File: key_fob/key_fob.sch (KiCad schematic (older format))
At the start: 21 parts

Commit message: Updated schmatic to include alarm off button
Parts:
- removed C? (x2): C, symbol Device:C
- removed U?: AMS1117-3.3, Package_TO_SOT_SMD:SOT-223-3_TabPin2, symbol Regulator_Linear:AMS1117-3.3
- added SW?: SW_DIP_x01, symbol Switch:SW_DIP_x01
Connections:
- net labels added: ALARM_OFF
- wire segments 40 -> 41
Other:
- moved on the sheet: D?, R?, SW?

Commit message: Added footprint and symbol library for some of the parts picked out
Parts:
- removed J?: Conn_01x02_Male, symbol Connector:Conn_01x02_Male
- removed LS?: Speaker, symbol Device:Speaker
- added C?: 2.2u, symbol Device:C
- added C?: 0.1u, symbol Device:C
- added IC?: L4931ABDT33-TR, TO228P972X240-3N, symbol SamacSys:L4931ABDT33-TR
- added J?: B2B-PH-K-S_LF__SN_, digikey-footprints:PinHeader_1x2_P2mm_Drill1mm, symbol digikey-kicad-library:B2B-PH-K-S_LF__SN_
- added U?: PS1240P02BT, PS1240P02BT, symbol PS1240P02BT:PS1240P02BT
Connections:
- net labels added: BUTTON0, POWER_LED
- net labels removed: ALARM_OFF
- wire segments 41 -> 55
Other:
- moved on the sheet: SW?

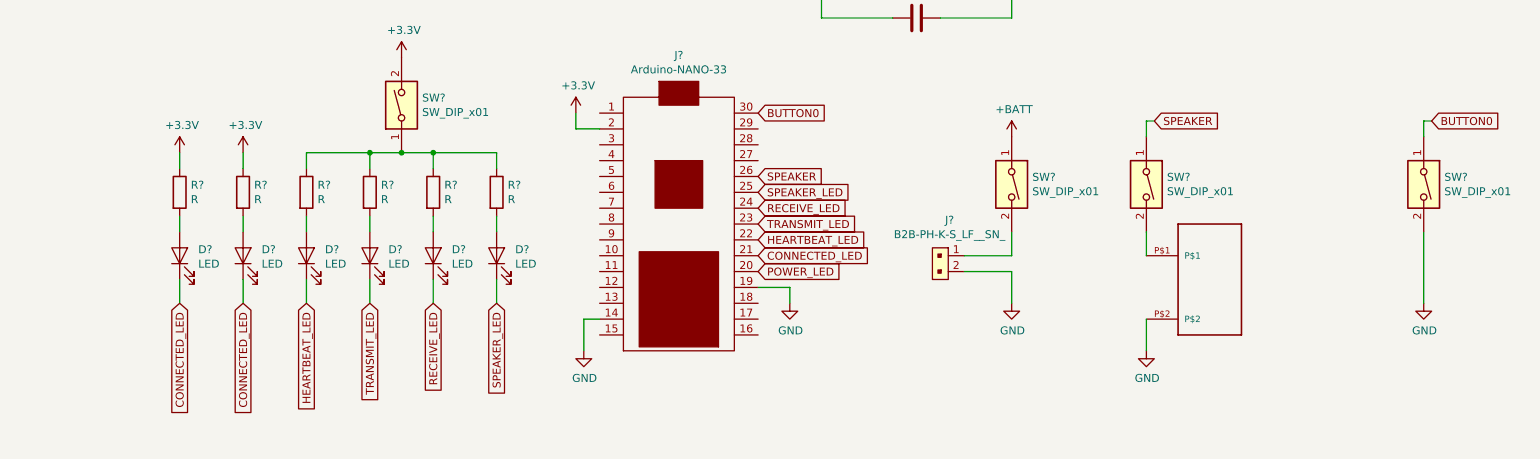
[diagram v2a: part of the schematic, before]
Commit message: Added Mosfets for External LEDs
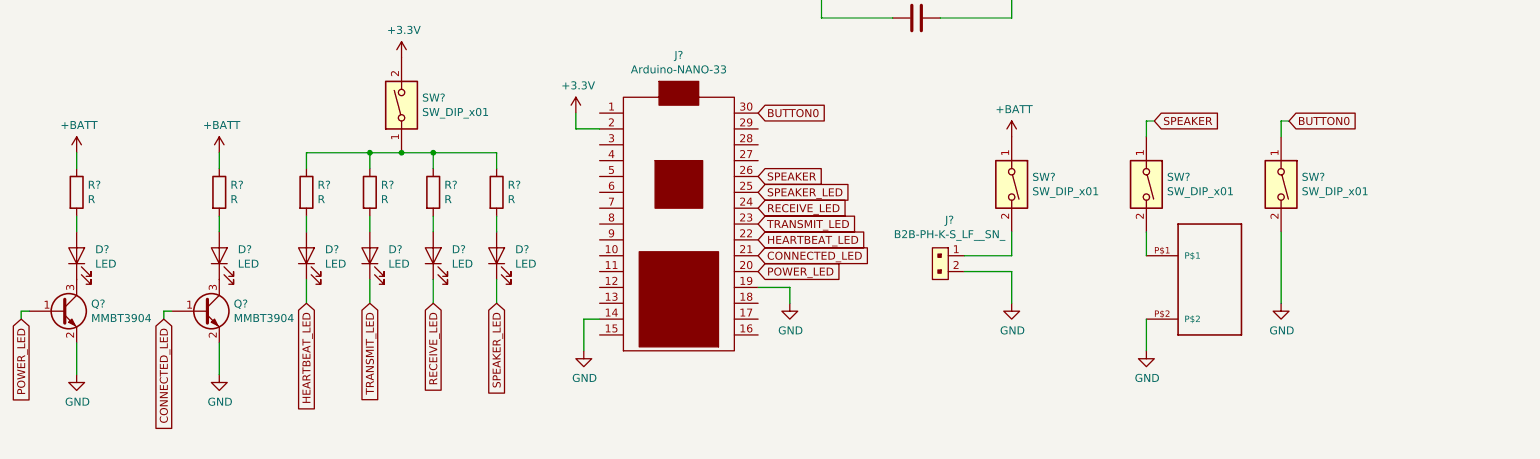
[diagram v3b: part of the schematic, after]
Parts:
- removed D? (x2): LED, symbol Device:LED
- removed R? (x2): R, symbol Device:R
- added D? (x2): LED, symbol Device:LED
- added Q? (x2): MMBT3904, Package_TO_SOT_SMD:SOT-23, symbol Transistor_BJT:MMBT3904
- added R? (x2): R, symbol Device:R
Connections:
- net +BATT: now also R?.1, R?.1
- net CONNECTED_LED: now also Q?.1 (B)
- net GND: now also Q?.2 (E), Q?.2 (E)
- net POWER_LED: now also Q?.1 (B)
- new net: D?.1 (K), Q?.3 (C) (x2)
- new net: D?.2 (A), R?.2 (x2)
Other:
- moved on the sheet: SW?
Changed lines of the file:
@@
 $EndDescr
-$Comp
-L Device:LED D?
-U 1 1 5E30F328
-P 2700 3800
-F 0 "D?" V 2739 3683 50  0000 R CNN
-F 1 "LED" V 2648 3683 50  0000 R CNN
-F 2 "" H 2700 3800 50  0001 C CNN
-F 3 "~" H 2700 3800 50  0001 C CNN
-	1    2700 3800
-	0    -1   -1   0
-$EndComp
-$Comp
-L Device:R R?
-U 1 1 5E3103C7
-P 2700 3400
-F 0 "R?" H 2770 3446 50  0000 L CNN
-F 1 "R" H 2770 3355 50  0000 L CNN
-F 2 "" V 2630 3400 50  0001 C CNN
-F 3 "~" H 2700 3400 50  0001 C CNN
-	1    2700 3400
-	1    0    0    -1
-$EndComp
-Wire Wire Line
-	2700 3550 2700 3650
-Wire Wire Line
-	2700 3250 2700 3150
-$Comp
-L Device:R R?
-U 1 1 5E319CBA
-P 3100 3400
-F 0 "R?" H 3170 3446 50  0000 L CNN
-F 1 "R" H 3170 3355 50  0000 L CNN
-F 2 "" V 3030 3400 50  0001 C CNN
-F 3 "~" H 3100 3400 50  0001 C CNN
-	1    3100 3400
-	1    0    0    -1
-$EndComp
 $Comp
 L Device:R R?
@@
 Wire Wire Line
 	3500 4100 3500 3950
-Wire Wire Line
-	3100 4100 3100 3950
-Text GLabel 3100 4100 3    50   Input ~ 0
+Text GLabel 2600 4200 3    50   Input ~ 0
 CONNECTED_LED
-$Comp
-L Device:LED D?
-U 1 1 5E319CB4
-P 3100 3800
-F 0 "D?" V 3139 3683 50  0000 R CNN
-F 1 "LED" V 3048 3683 50  0000 R CNN
-F 2 "" H 3100 3800 50  0001 C CNN
-F 3 "~" H 3100 3800 50  0001 C CNN
-	1    3100 3800
-	0    -1   -1   0
-$EndComp
-Wire Wire Line
-	3100 3550 3100 3650
 Text GLabel 6350 3600 2    50   Input ~ 0
 TRANSMIT_LED
@@
 Wire Wire Line
 	4700 3250 4700 3150
-$Comp
-L power:+3.3V #PWR?
-U 1 1 5E33A695
-P 2700 3150
-F 0 "#PWR?" H 2700 3000 50  0001 C CNN
-F 1 "+3.3V" H 2715 3323 50  0000 C CNN
-F 2 "" H 2700 3150 50  0001 C CNN
-F 3 "" H 2700 3150 50  0001 C CNN
-	1    2700 3150
-	1    0    0    -1
-$EndComp
-Wire Wire Line
-	3100 3250 3100 3150
-$Comp
-L power:+3.3V #PWR?
-U 1 1 5E33CA46
-P 3100 3150
-F 0 "#PWR?" H 3100 3000 50  0001 C CNN
-F 1 "+3.3V" H 3115 3323 50  0000 C CNN
-F 2 "" H 3100 3150 50  0001 C CNN
-F 3 "" H 3100 3150 50  0001 C CNN
-	1    3100 3150
-	1    0    0    -1
-$EndComp
 Wire Wire Line
 	8800 3650 8800 3800
@@
 Wire Wire Line
 	8800 2950 8800 3050
-Text GLabel 3500 4100 3    50   Input ~ 0
-HEARTBEAT_LED
 Text GLabel 3900 4100 3    50   Input ~ 0
 TRANSMIT_LED
@@
 $Comp
 L power:GND #PWR?
-U 1 1 5E333A60
-P 5250 4400
-F 0 "#PWR?" H 5250 4150 50  0001 C CNN
-F 1 "GND" H 5255 4227 50  0000 C CNN
-F 2 "" H 5250 4400 50  0001 C CNN
-F 3 "" H 5250 4400 50  0001 C CNN
-	1    5250 4400
-	1    0    0    -1
-$EndComp
-Wire Wire Line
-	5250 4200 5250 4400
-$Comp
-L power:GND #PWR?
 U 1 1 5E336757
 P 6550 4100
@@
 Wire Wire Line
 	5350 4200 5250 4200
-$Comp
-L Nano_33:Arduino-NANO-33 J?
-U 1 1 5E309CC1
-P 5850 3600
-F 0 "J?" H 5850 4665 50  0000 C CNN
-F 1 "Arduino-NANO-33" H 5850 4574 50  0000 C CNN
-F 2 "" H 5525 3500 50  0001 C CNN
-F 3 "~" H 5525 3500 50  0001 C CNN
-	1    5850 3600
-	1    0    0    -1
-$EndComp
 Text GLabel 6350 3700 2    50   Input ~ 0
 HEARTBEAT_LED
@@
 Text GLabel 6350 2900 2    50   Input ~ 0
 BUTTON0
-Text GLabel 10600 2950 2    50   Input ~ 0
+Text GLabel 9700 2950 2    50   Input ~ 0
 BUTTON0
 $Comp
 L Switch:SW_DIP_x01 SW?
 U 1 1 5E36D86D
-P 10550 3350
-F 0 "SW?" V 10504 3480 50  0000 L CNN
-F 1 "SW_DIP_x01" V 10595 3480 50  0000 L CNN
-F 2 "" H 10550 3350 50  0001 C CNN
-F 3 "~" H 10550 3350 50  0001 C CNN
-	1    10550 3350
+P 9650 3350
+F 0 "SW?" V 9604 3480 50  0000 L CNN
+F 1 "SW_DIP_x01" V 9695 3480 50  0000 L CNN
+F 2 "" H 9650 3350 50  0001 C CNN
+F 3 "~" H 9650 3350 50  0001 C CNN
+	1    9650 3350
 	0    1    1    0
 $EndComp
 Wire Wire Line
-	10600 2950 10550 2950
-Wire Wire Line
-	10550 2950 10550 3050
+	9700 2950 9650 2950
+Wire Wire Line
+	9650 2950 9650 3050
 $Comp
 L power:GND #PWR?
@@
 L power:GND #PWR?
 U 1 1 5E372BE7
-P 10550 4100
-F 0 "#PWR?" H 10550 3850 50  0001 C CNN
-F 1 "GND" H 10555 3927 50  0000 C CNN
-F 2 "" H 10550 4100 50  0001 C CNN
-F 3 "" H 10550 4100 50  0001 C CNN
-	1    10550 4100
-	1    0    0    -1
-$EndComp
-Wire Wire Line
-	10550 3650 10550 4100
+P 9650 4100
+F 0 "#PWR?" H 9650 3850 50  0001 C CNN
+F 1 "GND" H 9655 3927 50  0000 C CNN
+F 2 "" H 9650 4100 50  0001 C CNN
+F 3 "" H 9650 4100 50  0001 C CNN
+	1    9650 4100
+	1    0    0    -1
+$EndComp
+Wire Wire Line
+	9650 3650 9650 4100
 Text GLabel 6350 3900 2    50   Input ~ 0
 POWER_LED
-Text GLabel 2700 4100 3    50   Input ~ 0
-CONNECTED_LED
-Wire Wire Line
-	2700 3950 2700 4100
 $Comp
 L SamacSys:L4931ABDT33-TR IC?
@@
 	0    1    1    0
 $EndComp
+$Comp
+L Nano_33:Arduino-NANO-33 J?
+U 1 1 5E309CC1
+P 5850 3600
+F 0 "J?" H 5850 4665 50  0000 C CNN
+F 1 "Arduino-NANO-33" H 5850 4574 50  0000 C CNN
+F 2 "" H 5525 3500 50  0001 C CNN
+F 3 "~" H 5525 3500 50  0001 C CNN
+	1    5850 3600
+	1    0    0    -1
+$EndComp
+Wire Wire Line
+	5250 4200 5250 4400
+$Comp
+L power:GND #PWR?
+U 1 1 5E333A60
+P 5250 4400
+F 0 "#PWR?" H 5250 4150 50  0001 C CNN
+F 1 "GND" H 5255 4227 50  0000 C CNN
+F 2 "" H 5250 4400 50  0001 C CNN
+F 3 "" H 5250 4400 50  0001 C CNN
+	1    5250 4400
+	1    0    0    -1
+$EndComp
+$Comp
+L Device:LED D?
+U 1 1 5E4DA2B1
+P 2950 3800
+F 0 "D?" V 2989 3683 50  0000 R CNN
+F 1 "LED" V 2898 3683 50  0000 R CNN
+F 2 "" H 2950 3800 50  0001 C CNN
+F 3 "~" H 2950 3800 50  0001 C CNN
+	1    2950 3800
+	0    -1   -1   0
+$EndComp
+$Comp
+L Device:R R?
+U 1 1 5E4DA2B7
+P 2950 3400
+F 0 "R?" H 3020 3446 50  0000 L CNN
+F 1 "R" H 3020 3355 50  0000 L CNN
+F 2 "" V 2880 3400 50  0001 C CNN
+F 3 "~" H 2950 3400 50  0001 C CNN
+	1    2950 3400
+	1    0    0    -1
+$EndComp
+Wire Wire Line
+	2950 3550 2950 3650
+Wire Wire Line
+	2950 3250 2950 3150
+$Comp
+L power:+BATT #PWR?
+U 1 1 5E4DA2C6
+P 2950 3150
+F 0 "#PWR?" H 2950 3000 50  0001 C CNN
+F 1 "+BATT" H 2965 3323 50  0000 C CNN
+F 2 "" H 2950 3150 50  0001 C CNN
+F 3 "" H 2950 3150 50  0001 C CNN
+	1    2950 3150
+	1    0    0    -1
+$EndComp
+Wire Wire Line
+	2650 4150 2600 4150
+Wire Wire Line
+	2600 4150 2600 4200
+$Comp
+L power:GND #PWR?
+U 1 1 5E4DA2CD
+P 2950 4550
+F 0 "#PWR?" H 2950 4300 50  0001 C CNN
+F 1 "GND" H 2955 4377 50  0000 C CNN
+F 2 "" H 2950 4550 50  0001 C CNN
+F 3 "" H 2950 4550 50  0001 C CNN
+	1    2950 4550
+	1    0    0    -1
+$EndComp
+Wire Wire Line
+	2950 4350 2950 4550
+$Comp
+L Transistor_BJT:MMBT3904 Q?
+U 1 1 5E4DA2C0
+P 2850 4150
+F 0 "Q?" H 3041 4196 50  0000 L CNN
+F 1 "MMBT3904" H 3041 4105 50  0000 L CNN
+F 2 "Package_TO_SOT_SMD:SOT-23" H 3050 4075 50  0001 L CIN
+F 3 "https://www.fairchildsemi.com/datasheets/2N/2N3904.pdf" H 2850 4150 50  0001 L CNN
+	1    2850 4150
+	1    0    0    -1
+$EndComp
+Text GLabel 3500 4100 3    50   Input ~ 0
+HEARTBEAT_LED
+$Comp
+L Device:LED D?
+U 1 1 5E4E79F6
+P 2050 3800
+F 0 "D?" V 2089 3683 50  0000 R CNN
+F 1 "LED" V 1998 3683 50  0000 R CNN
+F 2 "" H 2050 3800 50  0001 C CNN
+F 3 "~" H 2050 3800 50  0001 C CNN
+	1    2050 3800
+	0    -1   -1   0
+$EndComp
+$Comp
+L Device:R R?
+U 1 1 5E4E79FC
+P 2050 3400
+F 0 "R?" H 2120 3446 50  0000 L CNN
+F 1 "R" H 2120 3355 50  0000 L CNN
+F 2 "" V 1980 3400 50  0001 C CNN
+F 3 "~" H 2050 3400 50  0001 C CNN
+	1    2050 3400
+	1    0    0    -1
+$EndComp
+Wire Wire Line
+	2050 3550 2050 3650
+Wire Wire Line
+	2050 3250 2050 3150
+$Comp
+L power:+BATT #PWR?
+U 1 1 5E4E7A04
+P 2050 3150
+F 0 "#PWR?" H 2050 3000 50  0001 C CNN
+F 1 "+BATT" H 2065 3323 50  0000 C CNN
+F 2 "" H 2050 3150 50  0001 C CNN
+F 3 "" H 2050 3150 50  0001 C CNN
+	1    2050 3150
+	1    0    0    -1
+$EndComp
+Wire Wire Line
+	1750 4150 1700 4150
+Wire Wire Line
+	1700 4150 1700 4200
+$Comp
+L power:GND #PWR?
+U 1 1 5E4E7A0C
+P 2050 4550
+F 0 "#PWR?" H 2050 4300 50  0001 C CNN
+F 1 "GND" H 2055 4377 50  0000 C CNN
+F 2 "" H 2050 4550 50  0001 C CNN
+F 3 "" H 2050 4550 50  0001 C CNN
+	1    2050 4550
+	1    0    0    -1
+$EndComp
+Wire Wire Line
+	2050 4350 2050 4550
+$Comp
+L Transistor_BJT:MMBT3904 Q?
+U 1 1 5E4E7A13
+P 1950 4150
+F 0 "Q?" H 2141 4196 50  0000 L CNN
+F 1 "MMBT3904" H 2141 4105 50  0000 L CNN
+F 2 "Package_TO_SOT_SMD:SOT-23" H 2150 4075 50  0001 L CIN
+F 3 "https://www.fairchildsemi.com/datasheets/2N/2N3904.pdf" H 1950 4150 50  0001 L CNN
+	1    1950 4150
+	1    0    0    -1
+$EndComp
+Text GLabel 1700 4200 3    50   Input ~ 0
+POWER_LED
 $EndSCHEMATC

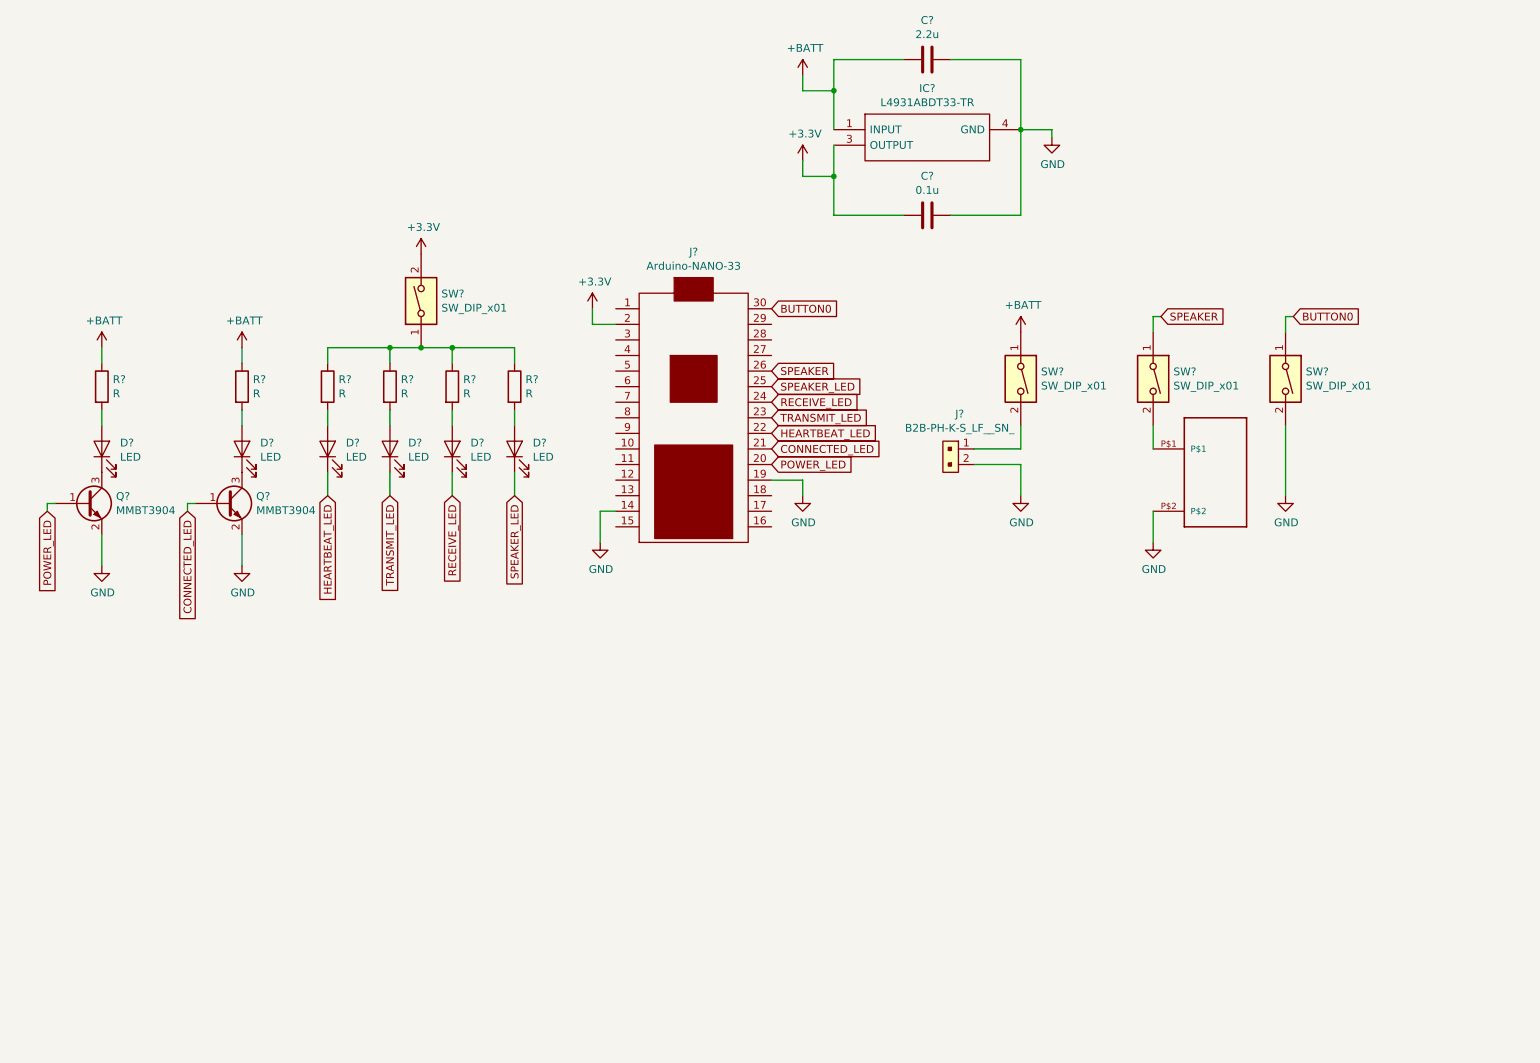
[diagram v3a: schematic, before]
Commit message: Linked all symbols to footprints
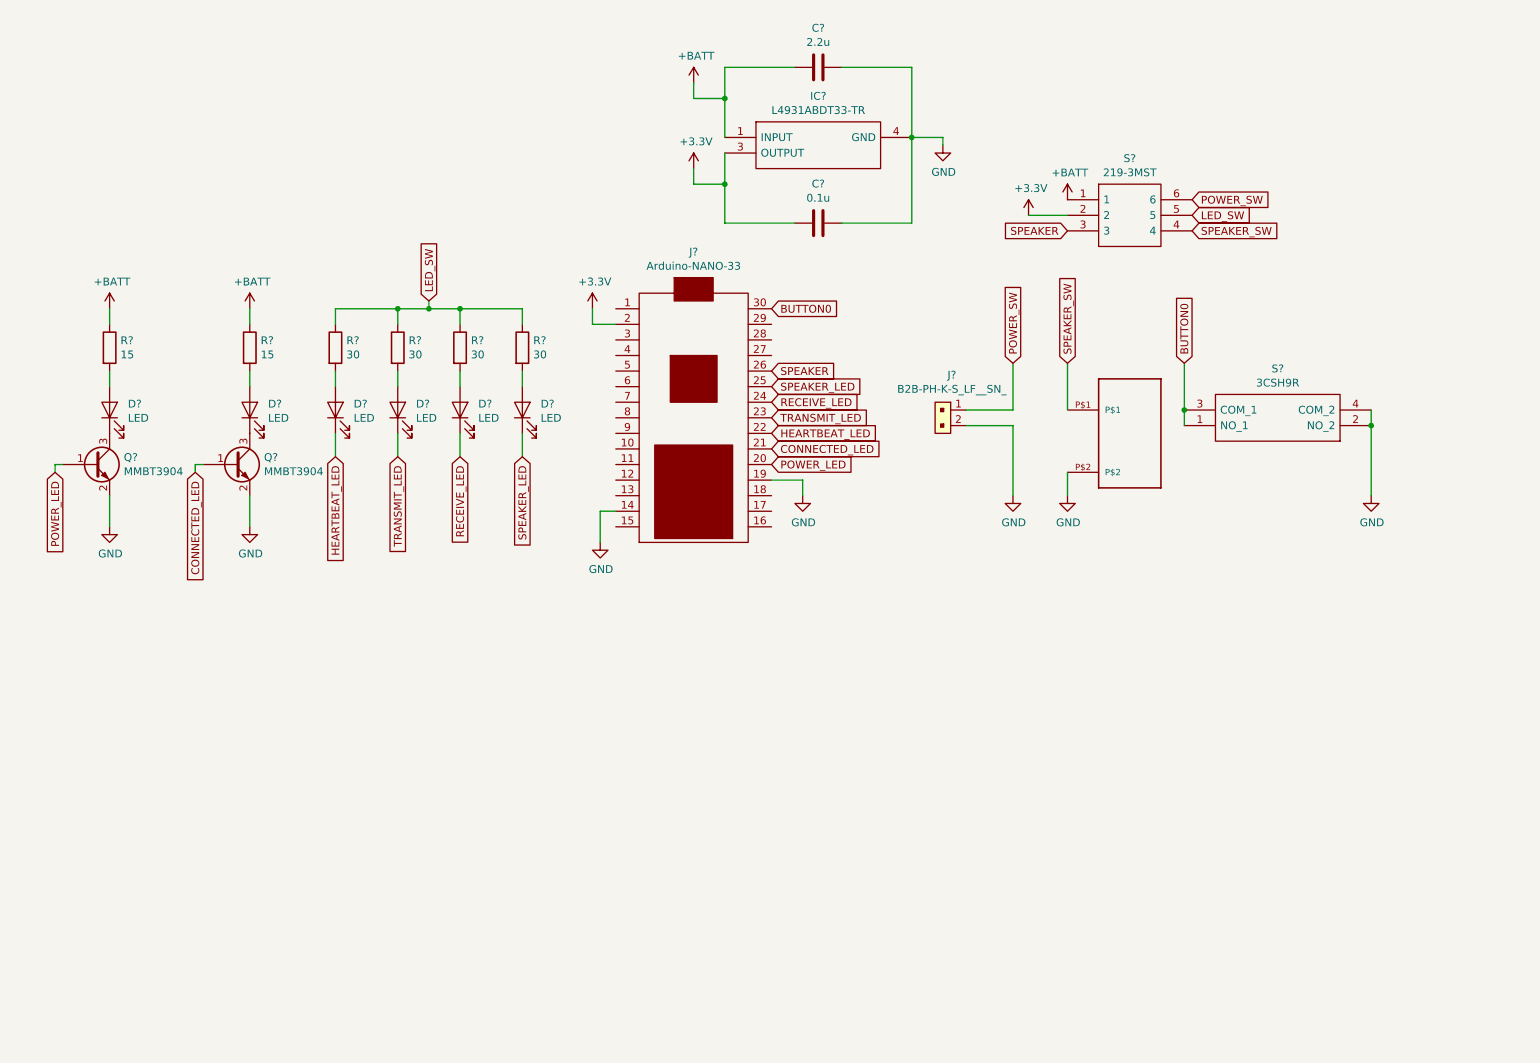
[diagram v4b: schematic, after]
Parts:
- removed J?: B2B-PH-K-S_LF__SN_, digikey-footprints:PinHeader_1x2_P2mm_Drill1mm, symbol digikey-kicad-library:B2B-PH-K-S_LF__SN_
- removed SW? (x4): SW_DIP_x01, symbol Switch:SW_DIP_x01
- added J?: B2B-PH-K-S_LF__SN_, digikey-kicad-library:PinHeader_1x2_P2mm_Drill1mm, symbol digikey-kicad-library:B2B-PH-K-S_LF__SN_
- added S?: 219-3MST, SamacSys:SOP254P991X385-6N, symbol SamacSys:219-3MST
- added S?: 3CSH9R, SamacSys:3CSH9R, symbol SamacSys:3CSH9R
- C? (x2): footprint (none) -> Capacitor_SMD:C_0603_1608Metric_Pad1.05x0.95mm_HandSolder
- D? (x4): footprint (none) -> LED_SMD:LED_1206_3216Metric_Pad1.42x1.75mm_HandSolder
- D? (x2): footprint (none) -> LED_THT:LED_D5.0mm
- IC?: footprint TO228P972X240-3N -> SamacSys:TO228P972X240-3N
- J?: footprint (none) -> Nano_33:NANO_33_Footprint_SMD_Castell
- R? (x4): value R -> 30; footprint (none) -> Resistor_SMD:R_0603_1608Metric_Pad1.05x0.95mm_HandSolder
- R? (x2): value R -> 15; footprint (none) -> Resistor_SMD:R_0603_1608Metric_Pad1.05x0.95mm_HandSolder
- U?: footprint PS1240P02BT -> PS1240P02BT:PS1240P02BT
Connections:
- net +3V3: now also S?.2
- net +BATT: now also S?.1
- net BUTTON0: now also S?.1 (NO_1), S?.3 (COM_1)
- net GND: now also J?.2, S?.2 (NO_2), S?.4 (COM_2)
- net SPEAKER: now also S?.3
- net LED_SW: now reaches R?.1, R?.1, R?.1, R?.1
- net LED_SW: now also S?.5
- net SPEAKER_SW: now reaches U?.P$1
- net SPEAKER_SW: now also S?.4
- new net POWER_SW: J?.1, S?.6
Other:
- moved on the sheet: C?, D?, IC?, Q?, R?
